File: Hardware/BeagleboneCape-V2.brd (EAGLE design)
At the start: 73.6 x 58.1 mm, 11 parts, among them P8 HEADER1, P9 HEADER2

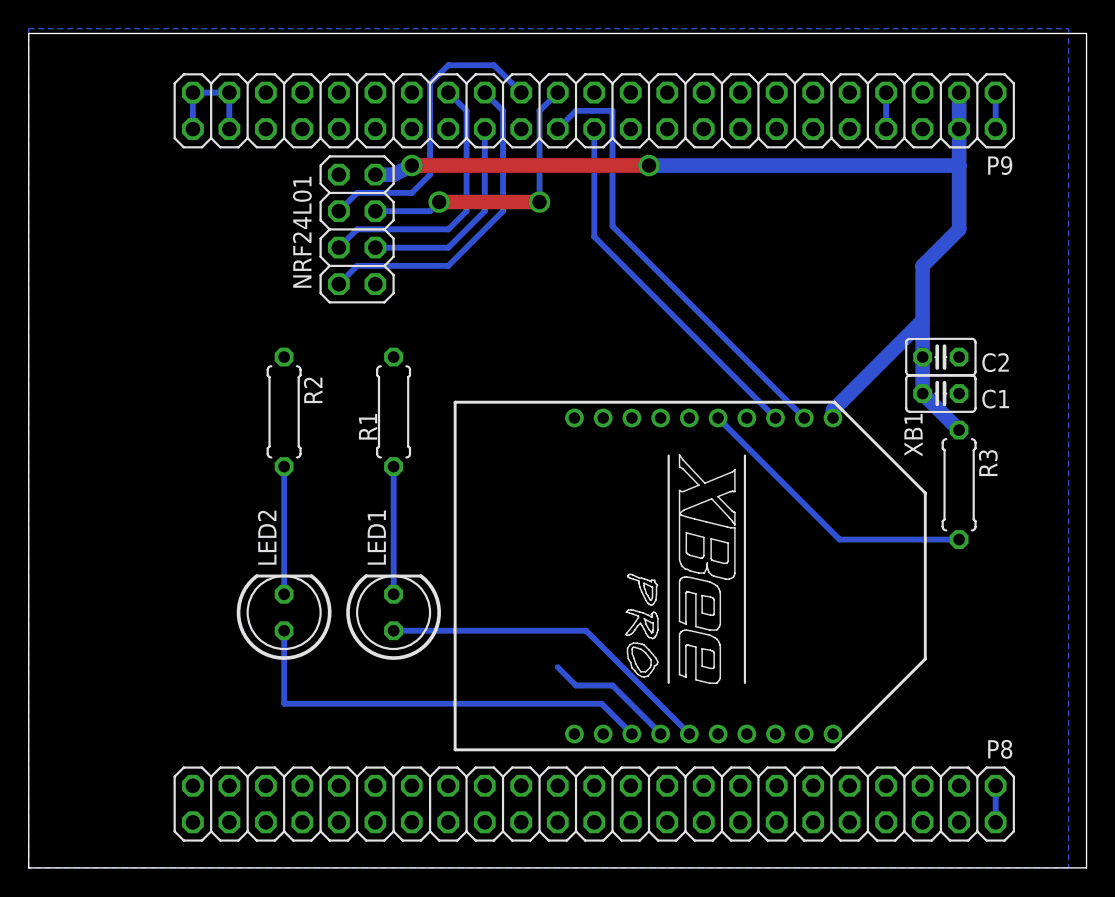
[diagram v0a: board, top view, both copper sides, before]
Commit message: updated cape after printout and generated V2 ( Rev B) SMD Version (prding completion on conversion).
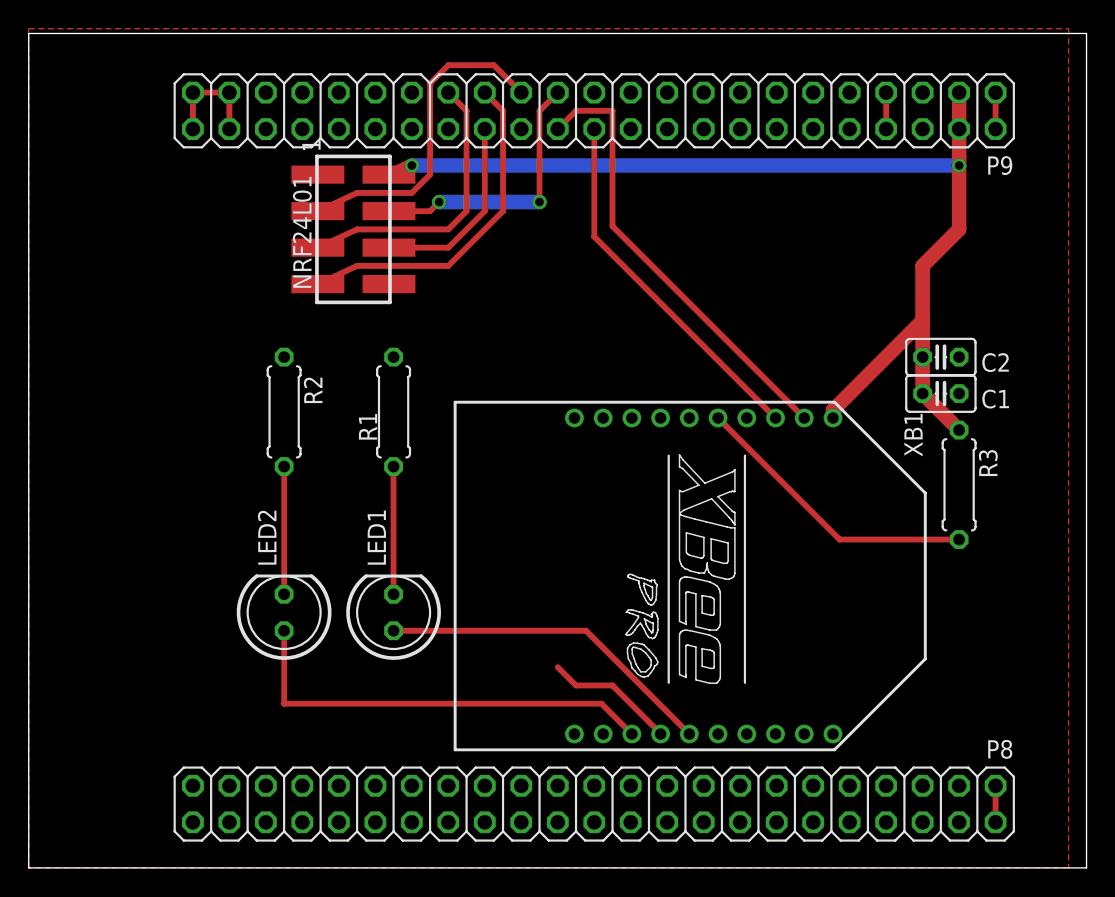
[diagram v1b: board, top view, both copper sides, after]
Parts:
- NRF24L01: device pinhead:2X04 -> Header:TSM-110-XX-XXX-DV
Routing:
- net SCK: track 18.7 -> 19.9 mm
- net MISO: track 22.3 -> 23.5 mm
- net CE: track 21.4 -> 22.6 mm
- net 3.3V: track 75.9 -> 75.0 mm
- net MOSI: track 14.4 -> 13.4 mm
- net CSN: track 19.8 -> 18.9 mm
- added copper zone on layer 1, net GND
- removed copper zone on layer 16, net GND

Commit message: updated V2 ( Rev B) Board to use SMD only components where possible. Using 1206 Components
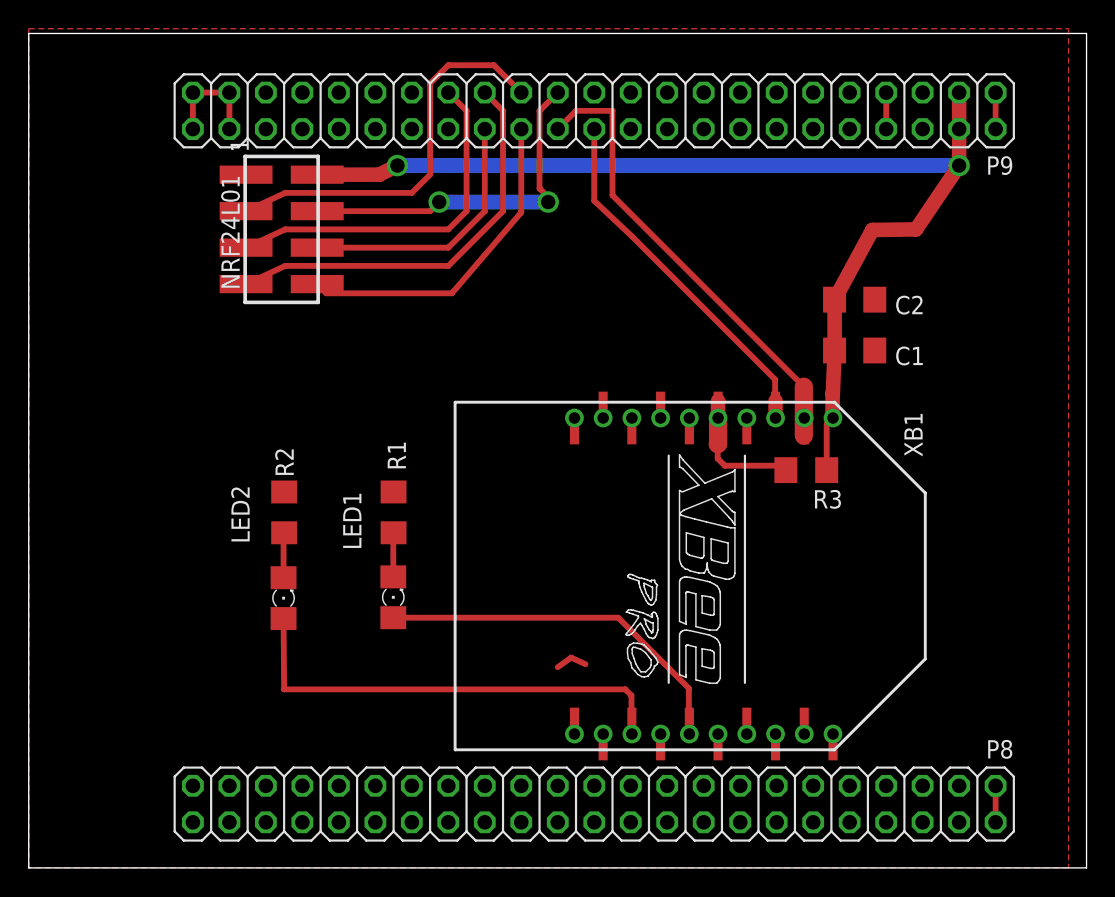
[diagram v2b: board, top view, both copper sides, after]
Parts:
- C1, C2: device rcl:C025-025X050 -> rcl:C1206
- LED1, LED2: device led:LED5MM -> led:1206
- R1, R2, R3: device rcl:0207/7 -> rcl:R1206
- moved R3 10.7 mm to (56.7, 27.7), turned to 180 degrees
- moved C2 7.21 mm to (60.0, 39.6)
- moved R1 7.00 mm to (27.9, 24.8)
- moved R2 7.00 mm to (20.3, 24.8)
- moved C1 6.71 mm to (60.0, 36.0)
- moved NRF24L01 5.00 mm to (20.4, 44.5)
- moved LED1 1.06 mm to (27.9, 18.8)
- moved LED2 1.00 mm to (20.3, 18.8)
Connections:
- net 3.3V: now also XB1.1-1
- net ASSOC: now also XB1.15-1
- net BB_RX: now also XB1.2-1
- net BB_TX: now also XB1.3-1
- net GND: now also XB1.10-1, XB1.14-1
- net IRQ: now also P9.28
- net N$1: now also LED1.C; no longer LED1.K
- net N$2: now also XB1.5-1
- net N$3: now also LED2.C; no longer LED2.K
- net ON_SLEEP: now also XB1.13-1
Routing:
- net IRQ: track 0.00 -> 22.9 mm
- net N$2: track 20.3 -> 9.14 mm
- net GND: track 21.8 -> 15.0 mm
- net N$1: track 9.11 -> 3.09 mm
- net CSN: track 18.9 -> 24.7 mm
- net N$3: track 8.89 -> 3.17 mm
- net SCK: track 19.9 -> 24.9 mm
- net MOSI: track 13.4 -> 18.4 mm
- net MISO: track 23.5 -> 28.5 mm
- net CE: track 22.6 -> 27.6 mm
- net ON_SLEEP: track 30.2 -> 33.2 mm
- net BB_RX: track 31.3 -> 33.8 mm
- net ASSOC: track 23.6 -> 25.8 mm
- net 3.3V: track 75.0 -> 75.9 mm
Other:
- board text added: "2015 Rev. B"
- board text removed: "2015 Rev. A"
